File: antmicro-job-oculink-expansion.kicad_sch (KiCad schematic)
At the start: 117 parts, among them J1 OCuLink_x4_Amphenol_G14A42121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, J2 Plug_Samtec_ERM8_2x40_ERM8-04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, U1 MAX3373EEKA+, U2 PI3EQX16904GL, U3 PI3EQX16904GL

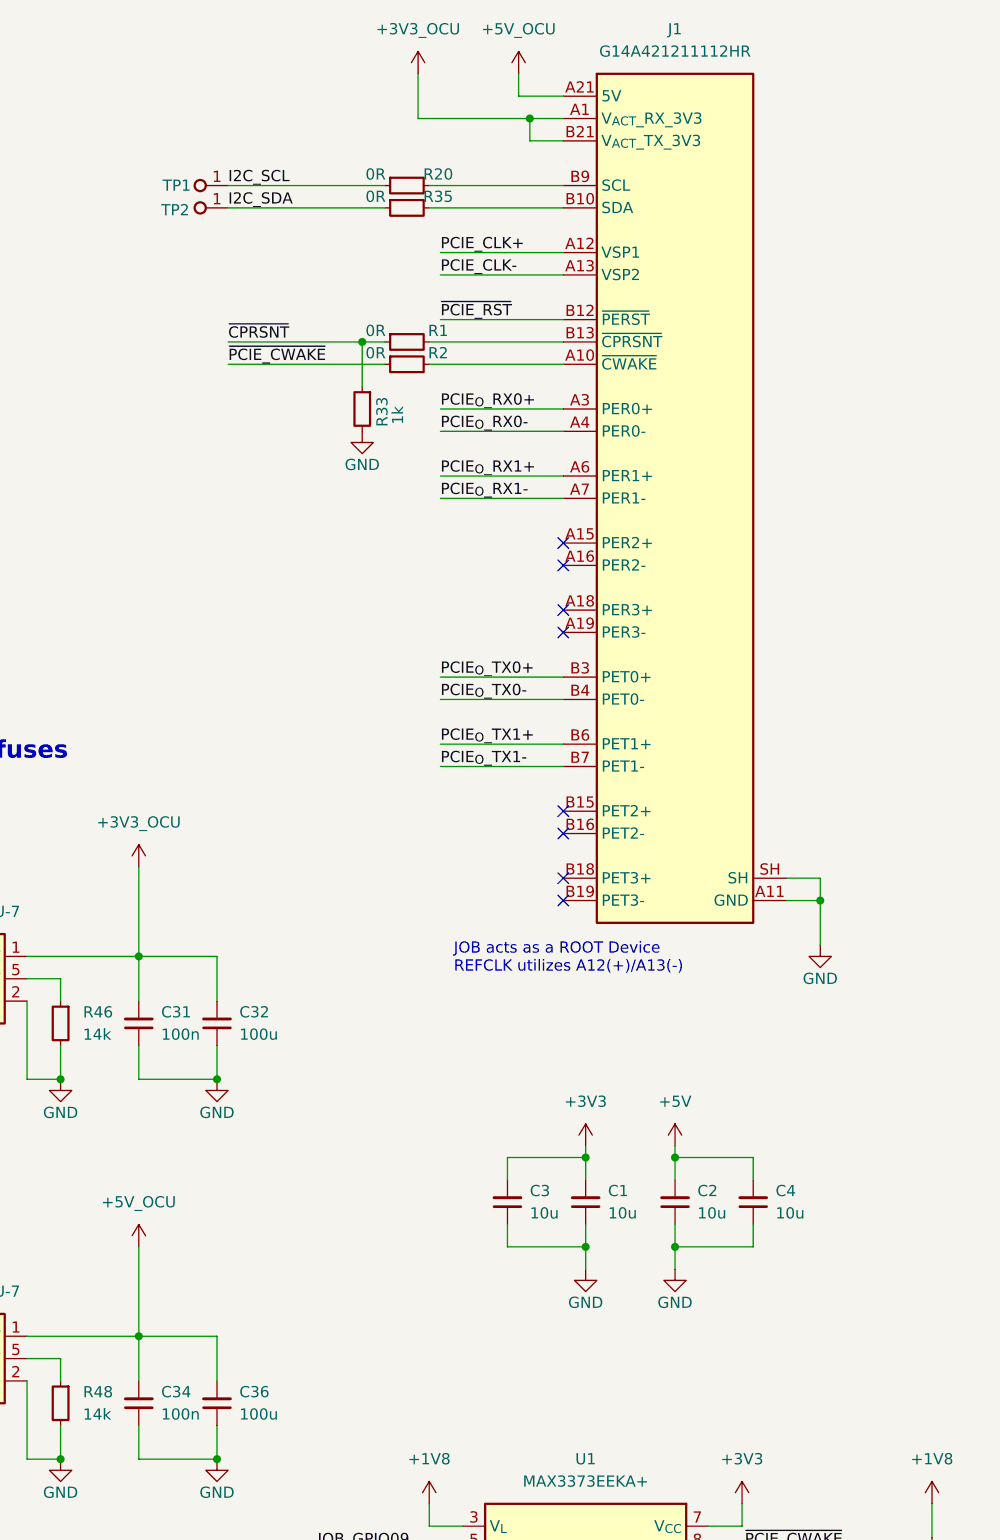
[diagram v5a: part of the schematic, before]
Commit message: [#77839] Connect OCuLink power through 0R resistors
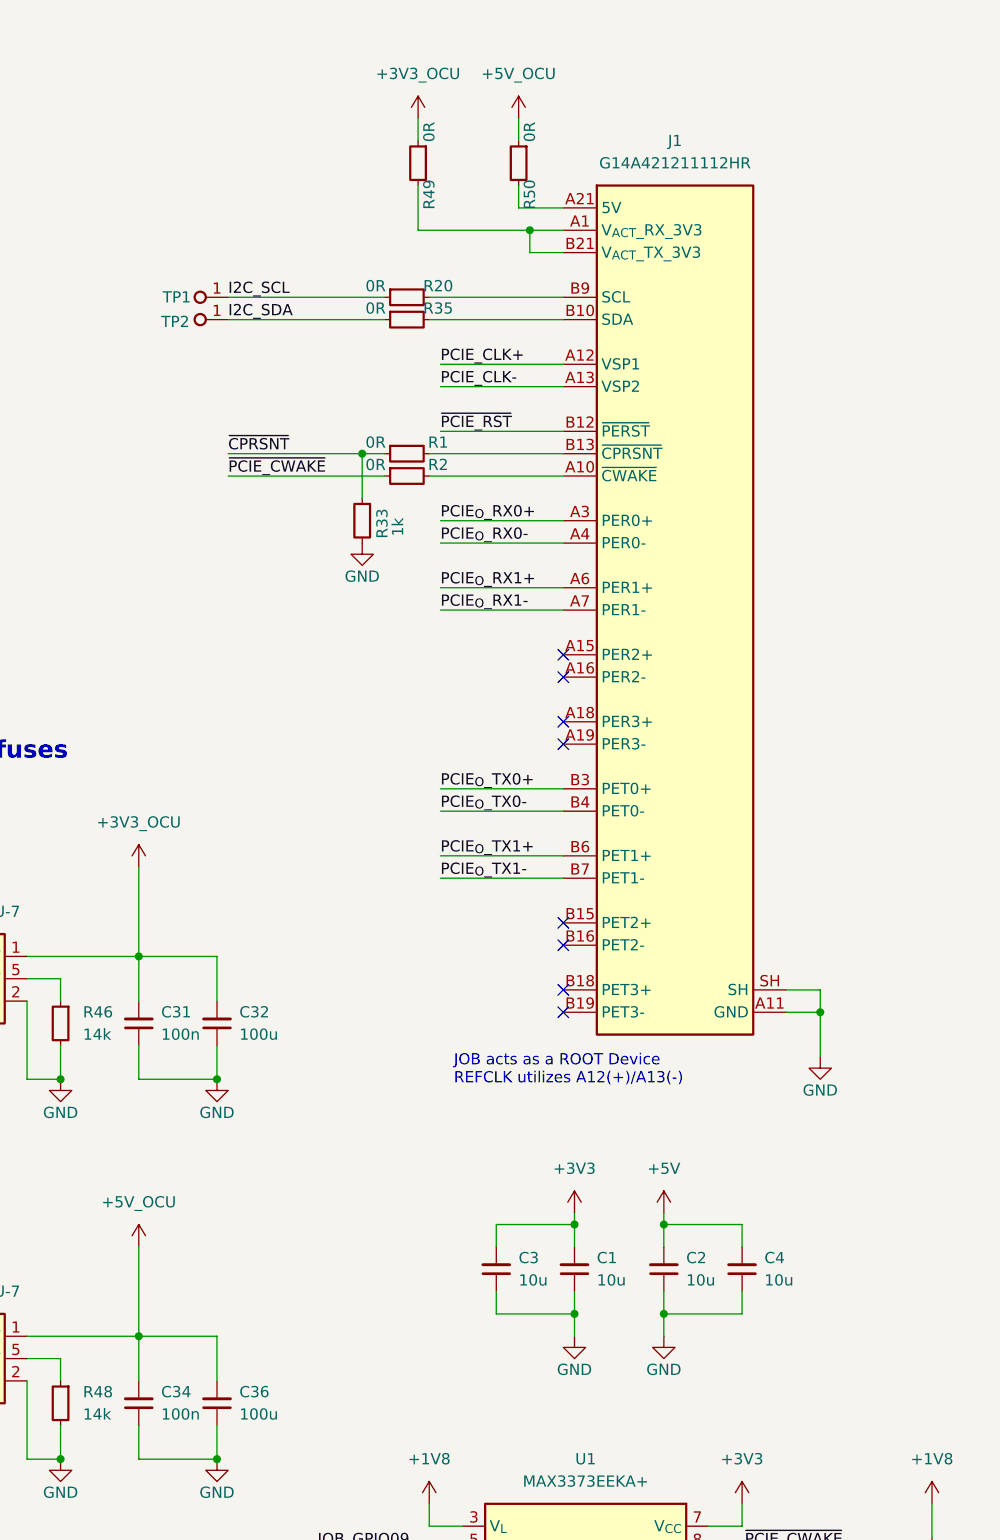
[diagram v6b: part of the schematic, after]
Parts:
- added R49, R50: R_0R_0402, antmicro-footprints:R_0402_1005Metric, symbol antmicroResistors0402:R_0R_0402
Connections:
- net +3V3_OCU: now also R49.1; no longer J1.A1 (V_{ACT}_RX_3V3), J1.B21 (V_{ACT}_TX_3V3)
- net +5V_OCU: now also R50.1; no longer J1.A21 (5V), J1.B1 (5V)
- new net: J1.A1 (V_{ACT}_RX_3V3), J1.B21 (V_{ACT}_TX_3V3), R49.2
- new net: J1.A21 (5V), J1.B1 (5V), R50.2
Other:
- moved on the sheet: C1, C2, C3, C4, J1, R1, R2, R20, R33, R35, TP1, TP2

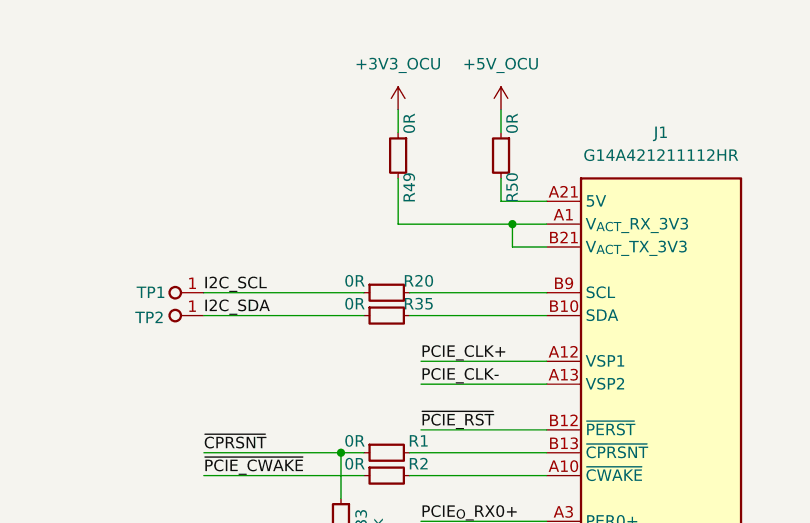
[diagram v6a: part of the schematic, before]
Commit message: [#77839] Add power flag to OCuLink 3V3 input
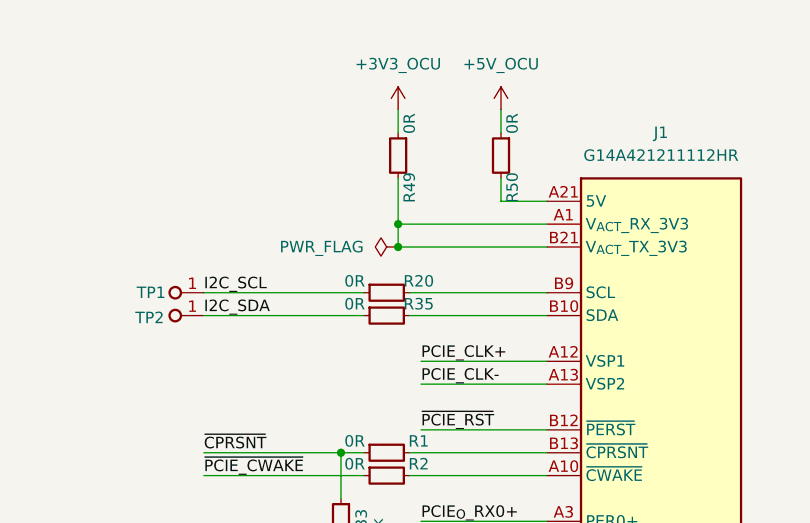
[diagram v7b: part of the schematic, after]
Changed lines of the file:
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@@
 	)
 	(junction
+		(at 327.66 43.18)
+		(diameter 0)
+		(color 0 0 0 0)
+	)
+	(junction
 		(at 57.15 60.96)
 		(diameter 0)
@@
 	)
 	(junction
-		(at 340.36 43.18)
+		(at 73.66 55.88)
 		(diameter 0)
 		(color 0 0 0 0)
 	)
 	(junction
-		(at 73.66 55.88)
+		(at 182.88 43.18)
 		(diameter 0)
 		(color 0 0 0 0)
 	)
 	(junction
-		(at 182.88 43.18)
+		(at 327.66 45.72)
 		(diameter 0)
 		(color 0 0 0 0)
@@
 	(wire
 		(pts
+			(xy 327.66 45.72) (xy 344.17 45.72)
+		)
+		(stroke
+			(width 0)
+			(type default)
+		)
+	)
+	(wire
+		(pts
 			(xy 149.86 130.81) (xy 149.86 133.35)
 		)
@@
 	(wire
 		(pts
-			(xy 340.36 43.18) (xy 344.17 43.18)
+			(xy 327.66 43.18) (xy 344.17 43.18)
 		)
 		(stroke
@@
 	(wire
 		(pts
-			(xy 327.66 43.18) (xy 340.36 43.18)
-		)
-		(stroke
-			(width 0)
-			(type default)
-		)
-	)
-	(wire
-		(pts
 			(xy 71.12 30.48) (xy 73.66 30.48)
 		)
@@
 	(wire
 		(pts
+			(xy 327.66 45.72) (xy 327.66 43.18)
+		)
+		(stroke
+			(width 0)
+			(type default)
+		)
+	)
+	(wire
+		(pts
 			(xy 252.73 63.5) (xy 273.05 63.5)
 		)
@@
 	(wire
 		(pts
-			(xy 340.36 45.72) (xy 340.36 43.18)
-		)
-		(stroke
-			(width 0)
-			(type default)
-		)
-	)
-	(wire
-		(pts
 			(xy 193.04 87.63) (xy 193.04 93.98)
 		)
@@
 	(wire
 		(pts
-			(xy 344.17 45.72) (xy 340.36 45.72)
-		)
-		(stroke
-			(width 0)
-			(type default)
-		)
-	)
-	(wire
-		(pts
 			(xy 149.86 106.68) (xy 149.86 109.22)
 		)
@@
 					(unit 1)
 				)
+			)
+		)
+	)
+	(symbol
+		(lib_id "antmicropower:PWR_FLAG")
+		(at 327.66 45.72 90)
+		(unit 1)
+		(exclude_from_sim no)
+		(in_bom yes)
+		(on_board yes)
+		(dnp no)
+		(fields_autoplaced yes)
+		(property "Reference" "#FLG05"
+			(at 325.755 45.72 0)
+			(effects
+				(font
+					(size 1.27 1.27)
+				)
+				(hide yes)
+			)
+		)
+		(property "Value" "PWR_FLAG"
+			(at 323.85 45.7199 90)
+			(effects
+				(font
+					(size 1.27 1.27)
+				)
+				(justify left)
+			)
+		)
+		(property "Footprint" ""
+			(at 327.66 45.72 0)
+			(effects
+				(font
+					(size 1.27 1.27)
+				)
+				(hide yes)
+			)
+		)
+		(property "Datasheet" ""
+			(at 327.66 45.72 0)
+			(effects
+				(font
+					(size 1.27 1.27)
+				)
+				(hide yes)
+			)
+		)
+		(property "Description" ""
+			(at 327.66 45.72 0)
+			(effects
+				(font
+					(size 1.27 1.27)
+				)
+				(hide yes)
+			)
+		)
+		(pin "1"
+		)
+		(instances
+			(project ""
+				(path "/195f80bc-f1ce-461e-9433-be011ba7464b"
+					(reference "#FLG05")
+					(unit 1)
+				)
